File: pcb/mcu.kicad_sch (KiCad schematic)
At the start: 25 parts, among them J4 TC2030, U1 W25Q128JVS, U2 RP2040, Y1 ABM8AIG-12.000MHZ-12-2Z-T3

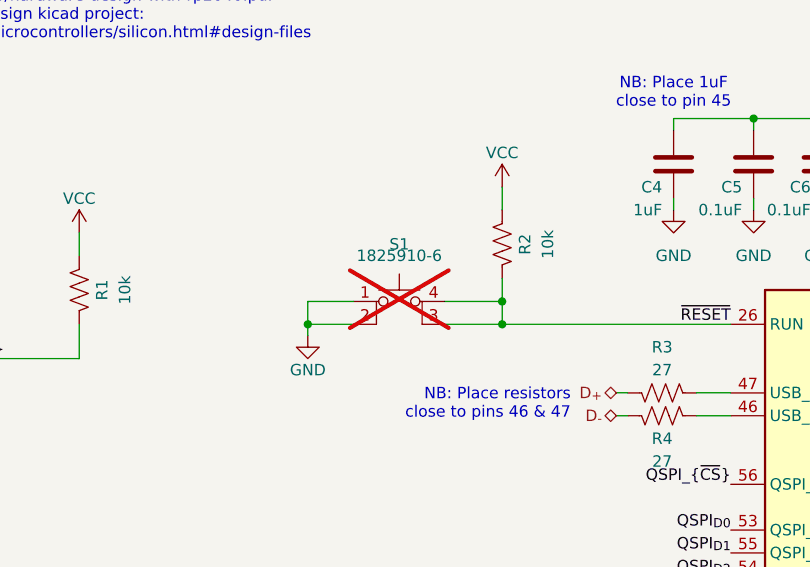
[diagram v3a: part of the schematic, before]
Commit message: Manual cleanup of repeated analog input array
- There was some manual cleanup needed
- Overall the repeated motif worked very well
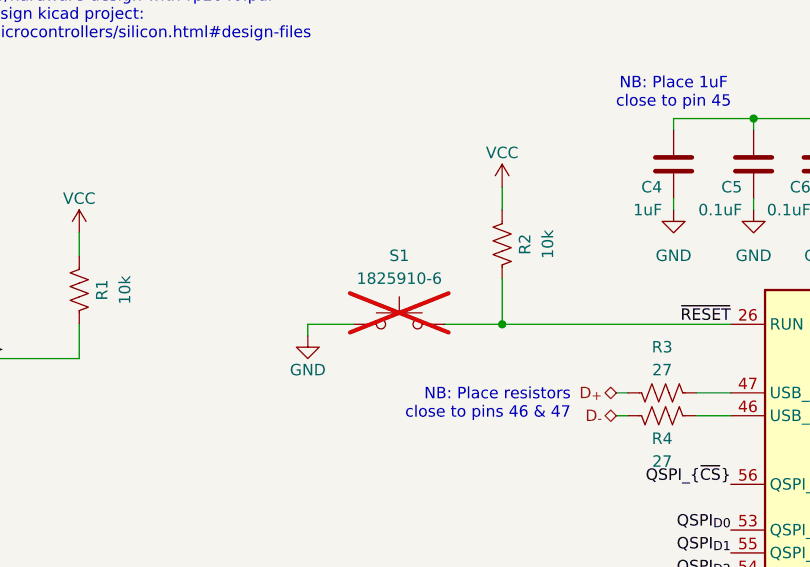
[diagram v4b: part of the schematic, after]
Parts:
- S1: symbol Switch:SW_MEC_5E -> Switch:SW_Push
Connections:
- net GND: no longer S1.2
- net ~{RESET}: now also S1.2; no longer S1.3 (K), S1.4 (A)
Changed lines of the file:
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@@
 	)
 	(junction
-		(at 111.76 60.96)
-		(diameter 0)
-		(color 0 0 0 0)
-	)
-	(junction
 		(at 243.84 38.1)
 		(diameter 0)
@@
 	)
 	(junction
-		(at 133.35 58.42)
-		(diameter 0)
-		(color 0 0 0 0)
-	)
-	(junction
 		(at 168.91 38.1)
 		(diameter 0)
@@
 	(wire
 		(pts
-			(xy 133.35 55.88) (xy 133.35 58.42)
+			(xy 133.35 55.88) (xy 133.35 60.96)
 		)
 		(stroke
@@
 	(wire
 		(pts
-			(xy 133.35 58.42) (xy 133.35 60.96)
-		)
-		(stroke
-			(width 0)
-			(type default)
-		)
-	)
-	(wire
-		(pts
 			(xy 154.94 71.12) (xy 158.75 71.12)
 		)
@@
 	(wire
 		(pts
-			(xy 116.84 58.42) (xy 111.76 58.42)
-		)
-		(stroke
-			(width 0)
-			(type default)
-		)
-	)
-	(wire
-		(pts
 			(xy 209.55 121.92) (xy 226.06 121.92)
 		)
@@
 	(wire
 		(pts
-			(xy 127 58.42) (xy 133.35 58.42)
-		)
-		(stroke
-			(width 0)
-			(type default)
-		)
-	)
-	(wire
-		(pts
 			(xy 147.32 68.58) (xy 146.05 68.58)
 		)
@@
 	(wire
 		(pts
-			(xy 111.76 58.42) (xy 111.76 60.96)
-		)
-		(stroke
-			(width 0)
-			(type default)
-		)
-	)
-	(wire
-		(pts
 			(xy 168.91 39.37) (xy 168.91 38.1)
 		)
@@
 	)
 	(symbol
-		(lib_id "Switch:SW_MEC_5E")
+		(lib_id "Switch:SW_Push")
 		(at 121.92 60.96 0)
 		(unit 1)
@@
 		(fields_autoplaced yes)
 		(property "Reference" "S1"
-			(at 121.92 52.07 0)
+			(at 121.92 53.34 0)
 			(effects
 				(font
@@
 		)
 		(property "Value" "1825910-6"
-			(at 121.92 53.34 0)
+			(at 121.92 55.88 0)
 			(effects
 				(font
@@
 		)
 		(property "Footprint" "Button_Switch_THT:SW_PUSH_6mm_H4.3mm"
-			(at 121.92 53.34 0)
+			(at 121.92 55.88 0)
 			(effects
 				(font
@@
 			)
 		)
-		(property "Datasheet" "http://www.apem.com/int/index.php?controller=attachment&id_attachment=1371"
-			(at 121.92 53.34 0)
+		(property "Datasheet" "~"
+			(at 121.92 55.88 0)
 			(effects
 				(font
@@
 			)
 		)
-		(property "Description" "MEC 5E single pole normally-open tactile switch"
+		(property "Description" "Push button switch, generic, two pins"
 			(at 121.92 60.96 0)
 			(effects
@@
 		(pin "2"
 		)
-		(pin "3"
-		)
-		(pin "4"
-		)
 		(instances

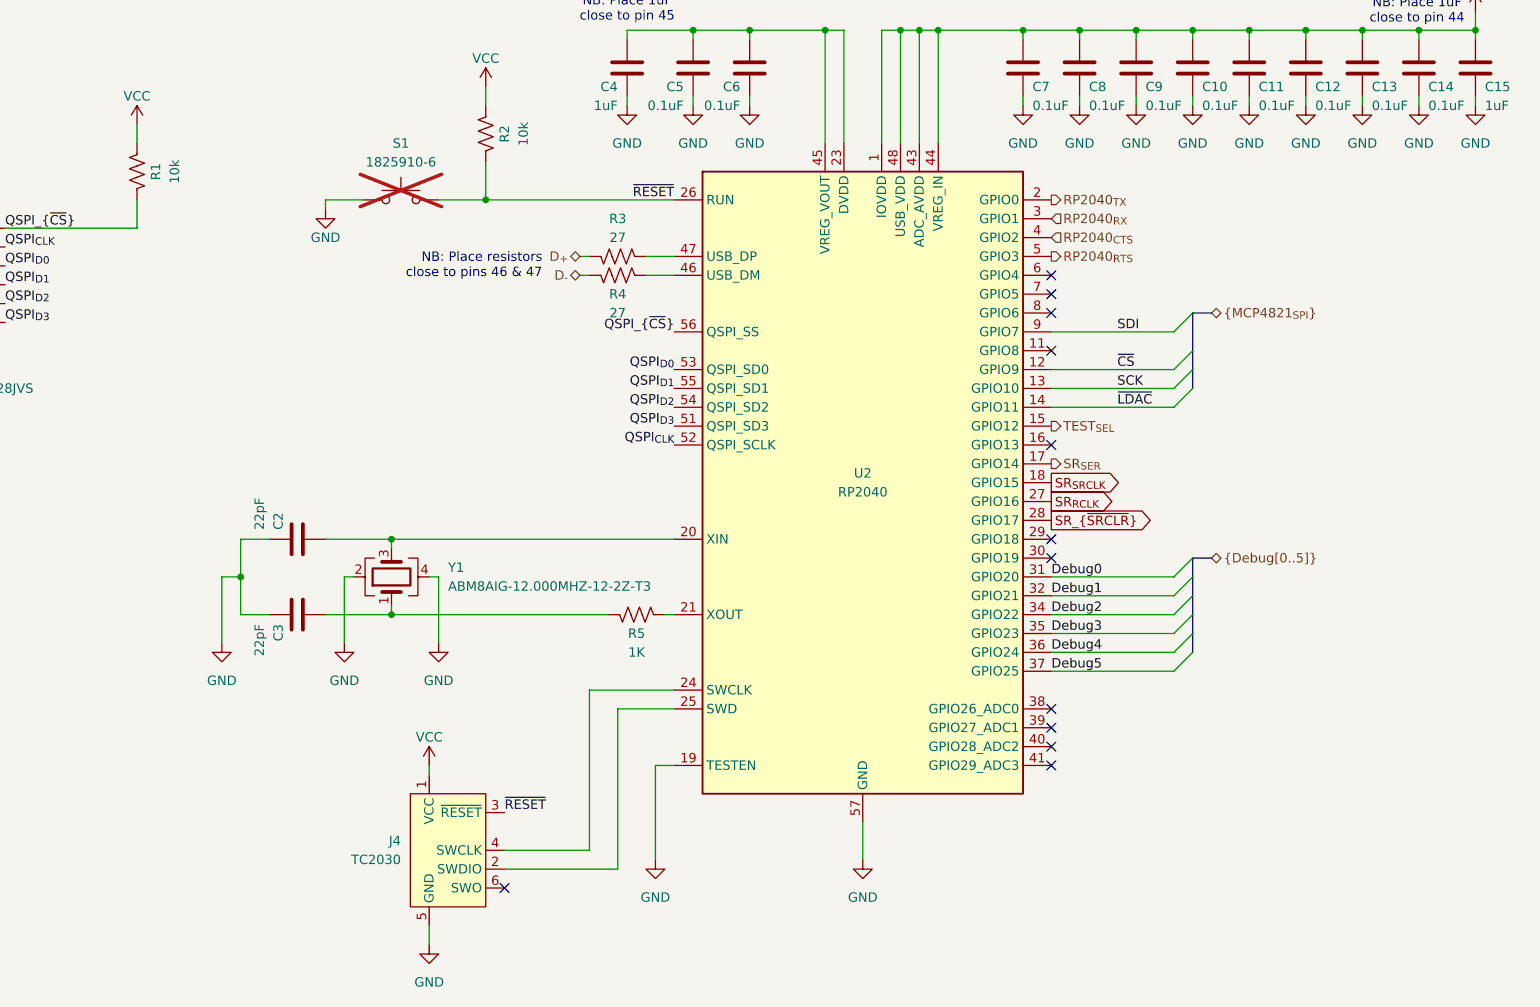
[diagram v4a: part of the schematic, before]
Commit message: Added user IO and battery
- Battery provides noise free operation
- OLED display and rotary encoder are not that hard to use
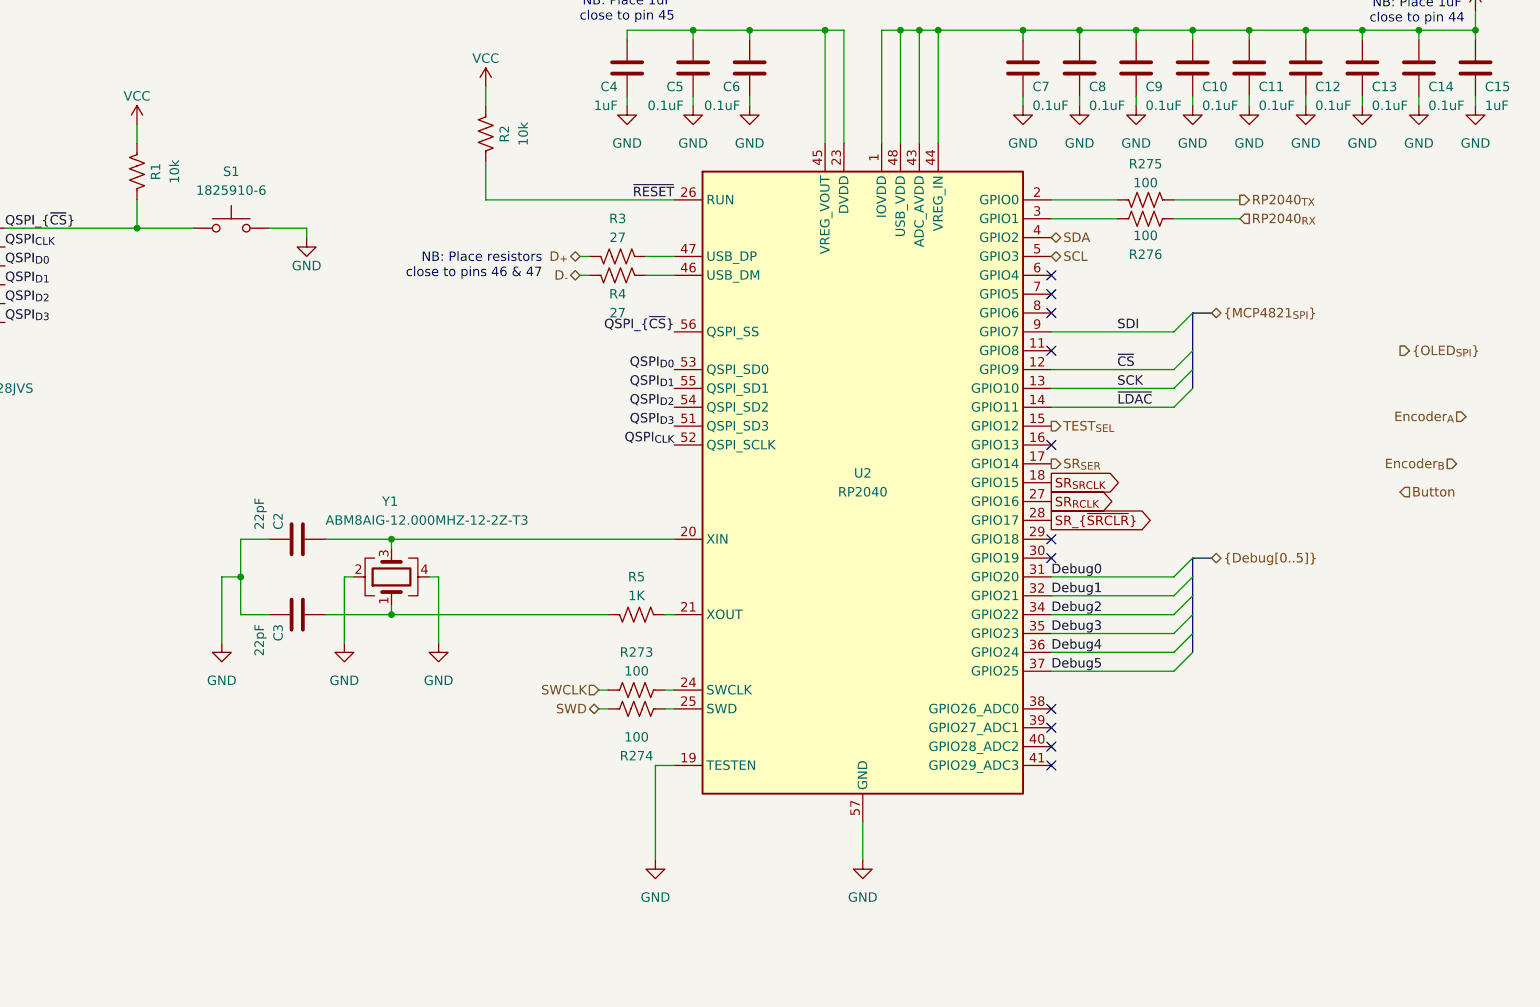
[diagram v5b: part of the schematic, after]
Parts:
- removed J4: TC2030, Connector:Tag-Connect_TC2030-IDC-FP_2x03_P1.27mm_Vertical, symbol Connector:Conn_ARM_SWD_TagConnect_TC2030
- added R273, R274, R275, R276: 100, Resistor_SMD:R_0402_1005Metric, symbol Device:R_US
- S1: now fitted
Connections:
- net QSPI_{~{CS}}: now also S1.2
- net RP2040_{RX}: now also R276.1; no longer U2.3 (GPIO1)
- net RP2040_{TX}: now also R275.1; no longer U2.2 (GPIO0)
- net ~{RESET}: no longer S1.2
- net at U2.25 (SWD): now also R274.1
- net at U2.24 (SWCLK): now also R273.2
- net RP2040_{CTS} renamed SDA
- net RP2040_{RTS} renamed SCL
- new net: R275.2, U2.2 (GPIO0)
- new net: R276.2, U2.3 (GPIO1)
- new net SWCLK: R273.1
- new net SWD: R274.2
- no-connect marks 12 -> 11

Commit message: Initial Rev. A schematic
- I think this has everything we need for revision A
- Battery charge indication via the OLED display
- User interface via rotary encoder/select switch
- Cycle through affected individual channels, none, or all
- Cycle through amplitudes
- Cycle through frequencies
- Select signal source
- Cycle through pre-loaded channel maps?
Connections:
- net Debug4 is gone; now on net Debug3: U2.36 (GPIO24)
- net Debug5 is gone; now on net ~{CS}: U2.37 (GPIO25)
- net Button: now also U2.31 (GPIO20)
- net Debug0: now also U2.32 (GPIO21); no longer U2.31 (GPIO20)
- net Debug1: now also U2.34 (GPIO22); no longer U2.32 (GPIO21)
- net Debug2: now also U2.35 (GPIO23); no longer U2.34 (GPIO22)
- net Debug3: no longer U2.35 (GPIO23)
- net Encoder_{A}: now also U2.29 (GPIO18)
- net Encoder_{B}: now also U2.30 (GPIO19)
- net ~{RESET}: now also U2.41 (GPIO29_ADC3)
- net SCLK: now reaches U2.38 (GPIO26_ADC0)
- net MOSI: now reaches U2.39 (GPIO27_ADC1)
- net ~{D/C}: now reaches U2.40 (GPIO28_ADC2)
- net VBus_{Detect}: now reaches U2.6 (GPIO4)
- net ~{Charging}: now reaches U2.7 (GPIO5)
- net SCL: no longer names the net of U2.5 (GPIO3)
- net SDA: no longer names the net of U2.4 (GPIO2)
- no-connect marks 11 -> 5
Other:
- note added: "RP2040 hardware design guide: https://datasheets.raspberrypi.com/rp2040/hardware-design-with-rp2040.pdf"
- note added: "SPI0"
- note added: "SPI1"
- note added: "Table 2 from Section 1.4.3. GPIO Functions, page 13"
- note added: "~{BOOT_SEL}"
- note removed: "rp2040 hardware design guide pdf: https://datasheets.raspberrypi.com/rp2040/hardware-design-with-rp2040.pdf minimial viable rp2040 design kicad project: https://www.raspberrypi.com/documentation/microcontrollers/silicon.html#design-files"
- moved on the sheet: C1, C10, C11, C12, C13, C14, C15, C2, C3, C4, C5, C6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

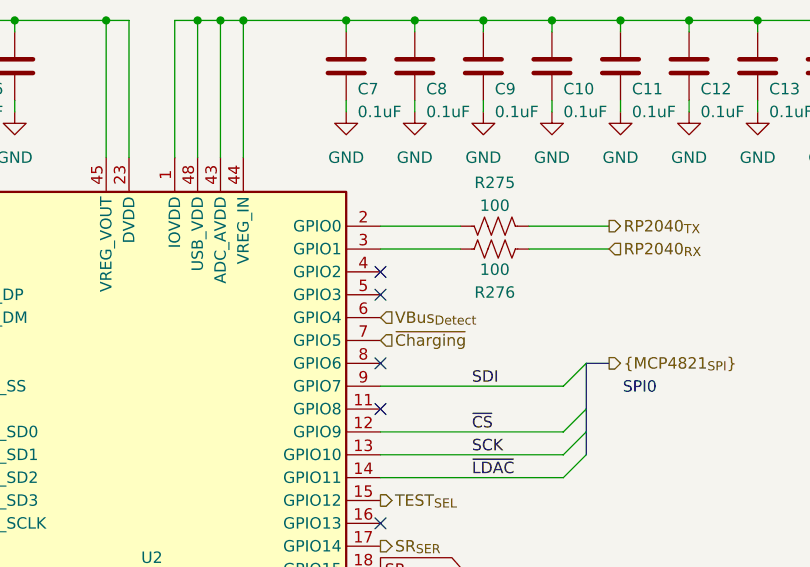
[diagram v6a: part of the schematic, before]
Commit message: Add EEPROM support to headstage interface
- I2C + Power
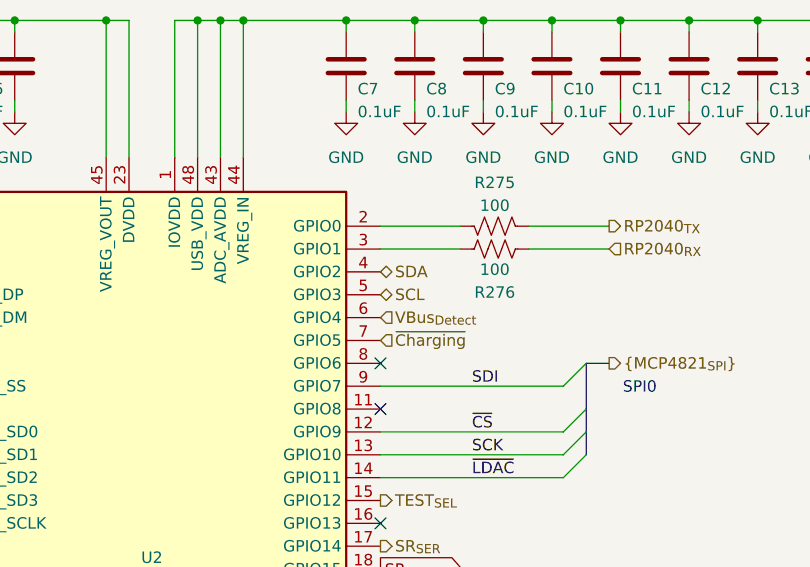
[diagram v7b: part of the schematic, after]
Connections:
- net SDA: now reaches U2.4 (GPIO2)
- net SCL: now reaches U2.5 (GPIO3)
- no-connect marks 5 -> 3
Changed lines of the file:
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@@
 	)
 	(no_connect
-		(at 163.83 66.04)
-	)
-	(no_connect
 		(at 163.83 78.74)
 	)
@@
 		(at 163.83 91.44)
 	)
-	(no_connect
-		(at 163.83 63.5)
-	)
 	(bus_entry
 		(at 186.69 127)
@@
 		)
 	)
+	(hierarchical_label "SCL"
+		(shape bidirectional)
+		(at 163.83 66.04 0)
+		(fields_autoplaced yes)
+		(effects
+			(font
+				(size 1.27 1.27)
+			)
+			(justify left)
+		)
+	)
 	(hierarchical_label "~{RESET}"
 		(shape input)
@@
 		)
 	)
+	(hierarchical_label "SDA"
+		(shape bidirectional)
+		(at 163.83 63.5 0)
+		(fields_autoplaced yes)
+		(effects
+			(font
+				(size 1.27 1.27)
+			)
+			(justify left)
+		)
+	)

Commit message: More schematic improvements
- Add pullups to i2c bus
- Add test points
- Ready for initial routing
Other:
- moved on the sheet: C1, C10, C11, C12, C13, C14, C15, C2, C3, C4, C5, C6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
